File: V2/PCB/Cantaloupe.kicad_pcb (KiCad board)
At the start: 2 copper layers, 143.9 x 118.7 mm, 118 parts, among them J1 USB_In, J2 OLED, J3 Link, J4 Debug, J5 Trackball, Q1 2N7002, Q2 AO3401A, SW1 MX, SW10 MX, SW11 MX, SW12 MX, SW13 MX, SW14 MX, SW15 MX, SW16 MX, SW17 MX, SW18 MX, SW19 MX, SW2 MX, SW20 MX, SW21 MX, SW22 MX, SW23 MX, SW24 MX, SW25 MX, SW26 MX, SW27 MX, SW28 MX, SW29 MX, SW3 MX, SW30 MX, SW31 Encoder, SW32 MX, SW4 MX, SW5 MX, SW6 MX, SW7 MX, SW8 MX, SW9 MX, U1 STM32F4x1CxUx, U2 SRV05-4, U3 SRV05-4, U4 XC6206P332MR, U5 LMV321, Y1 8MHz

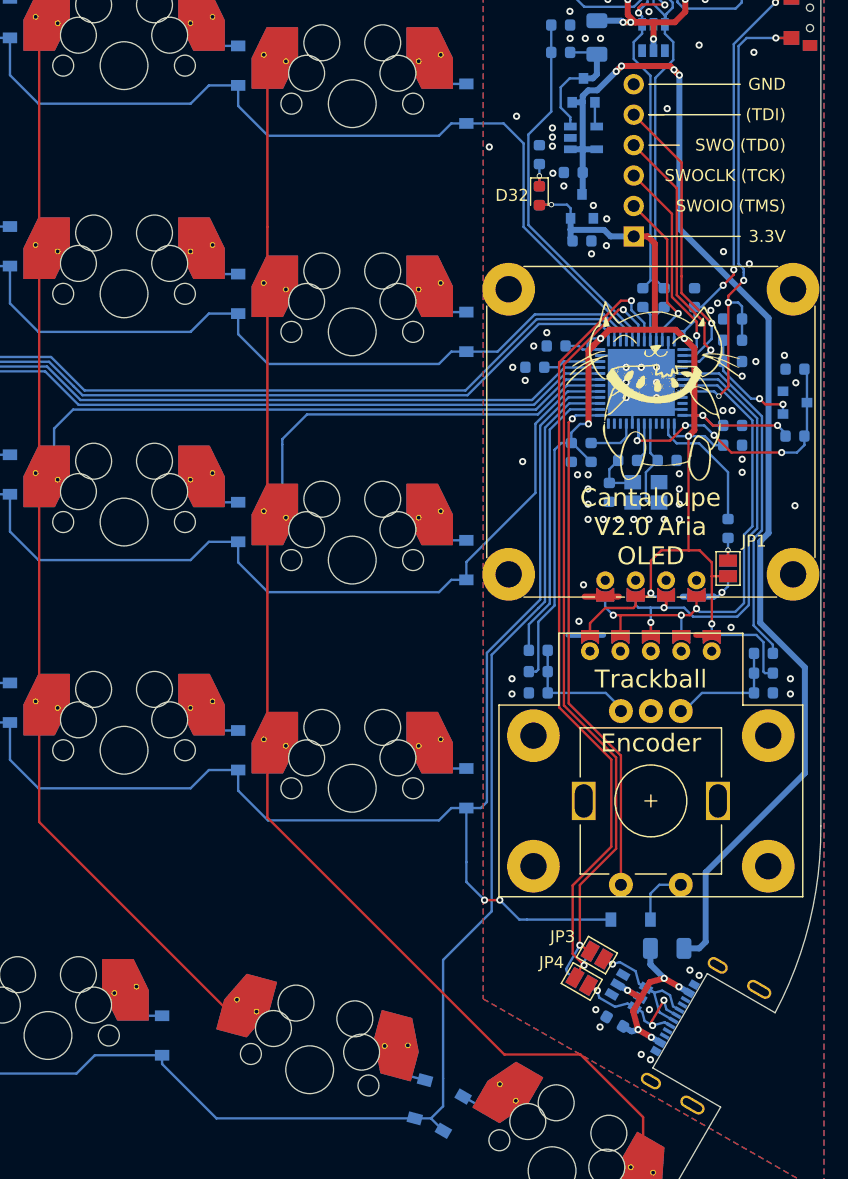
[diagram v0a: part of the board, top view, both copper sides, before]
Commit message: Fixed issues with PCB
Changed pin assignments so B2 isn't used. Added pull-up for RX pin and pull-down for B2 pin so it can properly load into the bootloader.
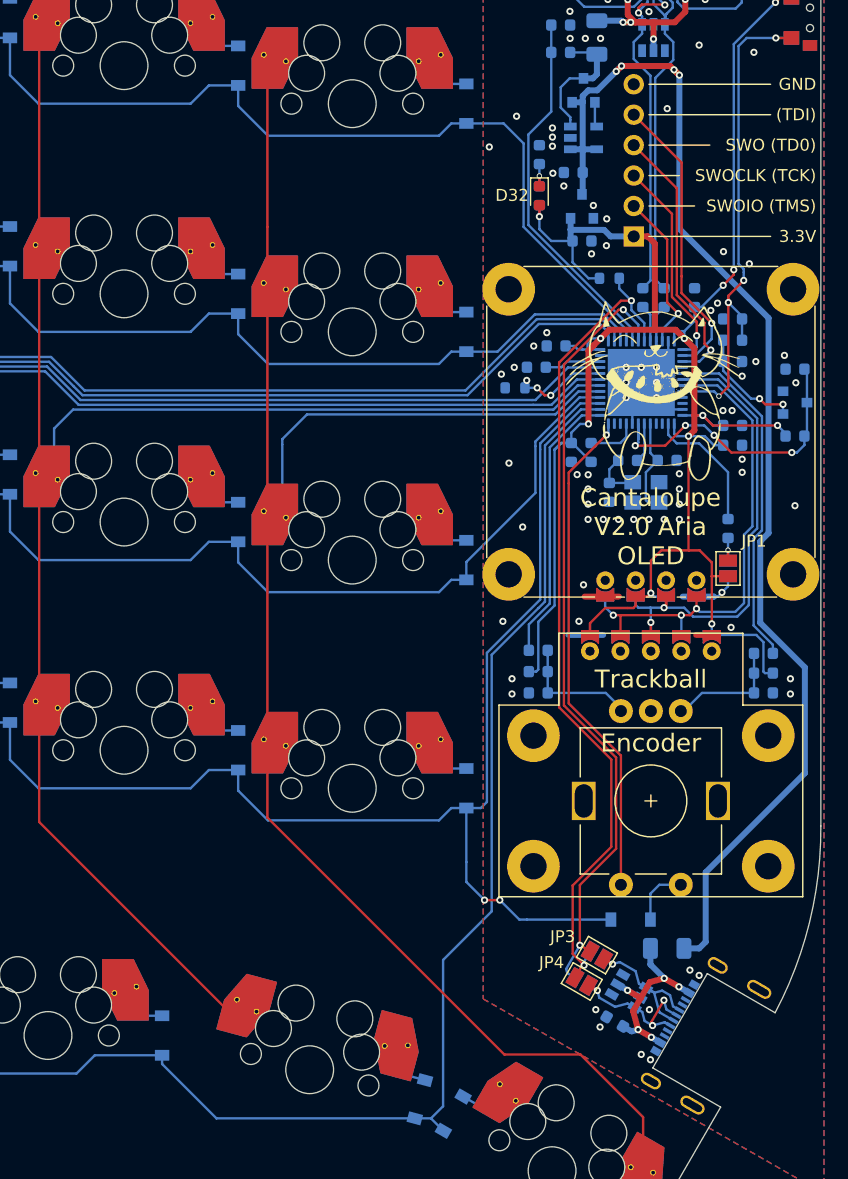
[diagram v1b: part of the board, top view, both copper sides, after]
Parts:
- added R18: 10k, Resistor_SMD:R_0603_1608Metric, B.Cu at (139.6, 44.9)
- added R4: 10k, Resistor_SMD:R_0603_1608Metric, B.Cu at (131.7, 54.0)
- moved C15 0.13 mm to (133.5, 52.3)
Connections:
- U1 pad 12: Net-(U1-Pad12) -> COLROT
- U1 pad 13: COLROT -> ROT_B
- U1 pad 14: ROT_B -> ROW4
- U1 pad 15: ROW4 -> ROW3
- U1 pad 16: ROW3 -> ROW2
- U1 pad 17: ROW2 -> COL5
- U1 pad 18: COL5 -> COL4
- U1 pad 19: COL4 -> COL3
- U1 pad 20: COL3 -> Net-(R4-Pad1)
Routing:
- net VDD: track 172.5 -> 180.1 mm
- net Net-(R4-Pad1): track 0.00 -> 7.29 mm, vias 0 -> 2
- net RX: track 68.5 -> 70.8 mm
- net COLROT: track 43.3 -> 41.7 mm
- net ROT_B: track 24.0 -> 23.0 mm
- net ROW4: track 169.6 -> 168.5 mm
- net ROW3: track 168.5 -> 167.4 mm
- net ROW2: track 129.7 -> 128.6 mm
- net NRST: track 25.0 -> 25.8 mm
- net GND: vias 84 -> 87
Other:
- rule pad_to_mask_clearance: 0.051 -> 0

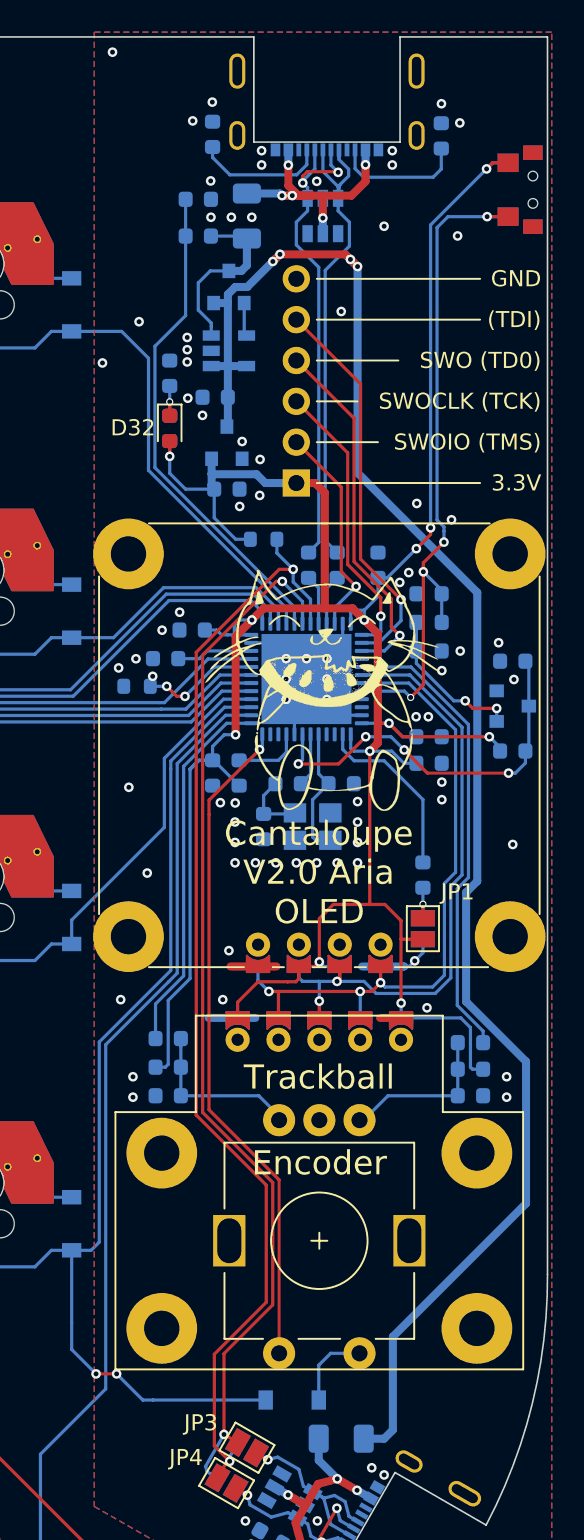
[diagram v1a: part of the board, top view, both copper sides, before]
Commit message: Fixed many issues with the board
Changed pin assignments so B2 isn't used. Added pull-up for RX pin and pull-down for B2 pin so the keyboard can properly load into the bootloader. Changed reset circuit so it actually works. Removed USB series resistors. Removed non-functional JTAG pins. Changed SRV05-04 to SRV0504. Thanks to sigprof and MasterSpoon from the QMK discord server for the help!
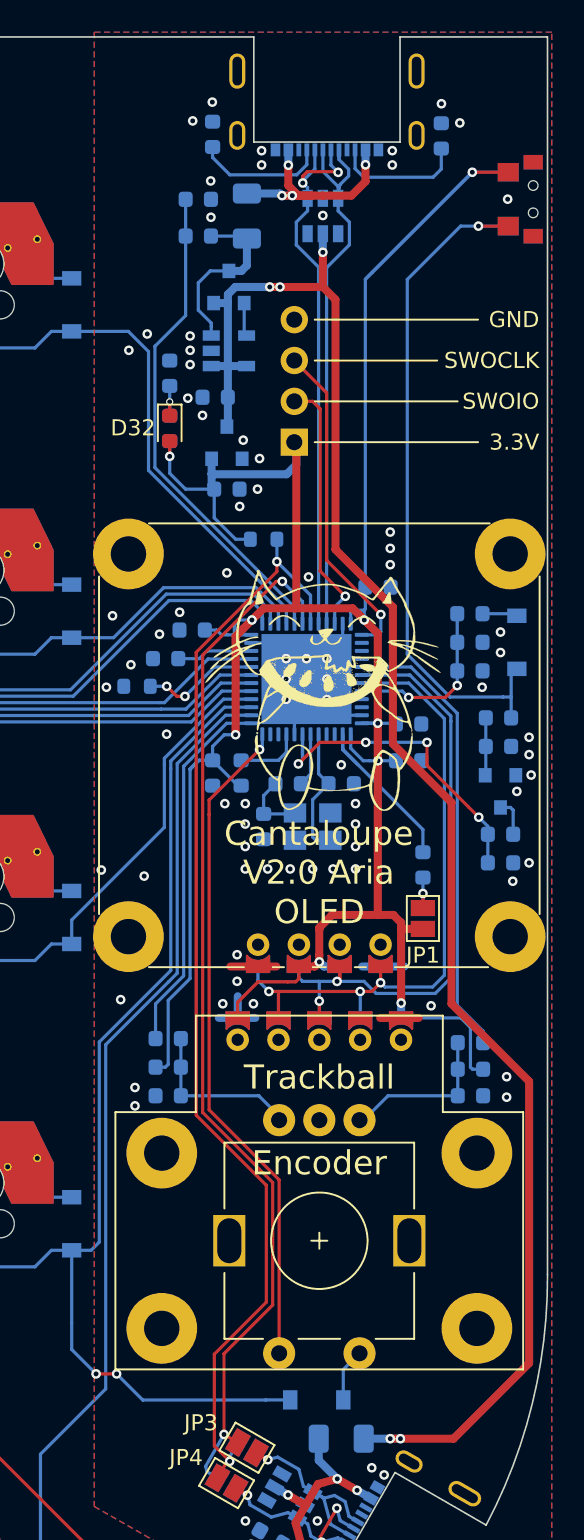
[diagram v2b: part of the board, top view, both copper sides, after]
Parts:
- added D33: D, Ariamelon:D_SOD-123, B.Cu at (155.3, 51.3)
- D32: moved to B.Cu
- R11: value 10k -> 1M
- R18, R4: value 10k -> 100k
- R2: value 10 -> 330k
- R3: value 10 -> 1k
- R9: value 100k -> 100
- U2, U3: value SRV05-4 -> SRV0504
- moved R3 13.8 mm to (154.2, 56.0), turned to 180 degrees
- moved C4 12.6 mm to (154.3, 65.0), turned to 180 degrees
- moved R9 12.2 mm to (154.3, 63.2), turned to 180 degrees
- moved R2 10.5 mm to (152.4, 49.5), turned to 0 degrees
- moved R7 10.4 mm to (154.2, 57.8), turned to 180 degrees
- moved R11 5.65 mm to (152.4, 53.1)
- moved Q1 5.36 mm to (154.3, 60.6), turned to 270 degrees
- moved C2 2.83 mm to (152.4, 51.3)
- moved D31 1.52 mm to (142.9, 98.4)
- moved C9 1.50 mm to (148.6, 56.4)
- moved C8 1.37 mm to (146.7, 47.9), turned to 180 degrees
- moved C14 1.28 mm to (148.6, 58.7)
- moved R16 0.64 mm to (149.5, 65.2)
- moved JP1 0.63 mm to (149.5, 68.5)
- moved JP2 0.63 mm to (149.5, 68.5)
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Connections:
- net JTCK renamed SWOCLK
- net JTMS renamed SWOIO
- C2 pad 1: Net-(C2-Pad1) -> BOOT0
- C2 pad 2: BOOT0 -> GND
- J4 pad 4: JTD0 -> GND
- Q1 pad 1: Net-(C2-Pad1) -> Net-(Q1-Pad1)
- Q1 pad 3: NRST -> Net-(Q1-Pad3)
- R11 pad 1: VDD -> BOOT0
- R11 pad 2: NRST -> GND
- R2 pad 1: D- -> BOOT0
- R2 pad 2: Net-(R2-Pad2) -> Net-(D33-Pad1)
- R3 pad 1: D+ -> Net-(D33-Pad2)
- R3 pad 2: Net-(R3-Pad2) -> Net-(Q1-Pad1)
- R7 pad 2: BOOT0 -> Net-(Q1-Pad1)
- R9 pad 1: Net-(C2-Pad1) -> Net-(Q1-Pad3)
- R9 pad 2: GND -> NRST
- SW32 pad 1: BOOT0 -> Net-(D33-Pad2)
- U1 pad 32: Net-(R2-Pad2) -> D-
- U1 pad 33: Net-(R3-Pad2) -> D+
- U1 pad 38: JTDI -> Net-(U1-Pad38)
- U1 pad 39: JTD0 -> Net-(U1-Pad39)
- U2 pad 5: VBUS -> VBUS_In
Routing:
- net Net-(D33-Pad2): track 0.00 -> 43.9 mm, vias 0 -> 1
- net BOOT0: track 43.1 -> 10.9 mm, vias 4 -> 2
- net JTDI: track 24.4 -> 0.00 mm, vias 1 -> 0
- net JTD0: track 22.5 -> 0.00 mm, vias 1 -> 0
- net Net-(C2-Pad1): track 9.51 -> 0.00 mm, vias 2 -> 0
- net VDD: track 180.1 -> 185.7 mm, vias 12 -> 9
- net NRST: track 25.8 -> 20.9 mm
- net D-: track 30.9 -> 35.1 mm
- net D+: track 30.1 -> 34.2 mm
- net Net-(Q1-Pad1): track 0.00 -> 3.59 mm
- net VBUS_In: track 105.4 -> 108.6 mm, vias 4 -> 5
- net Net-(R3-Pad2): track 3.13 -> 0.00 mm
- net Net-(R2-Pad2): track 3.11 -> 0.00 mm
- net SWOIO: track 13.4 -> 16.1 mm
- net SWOCLK: track 17.8 -> 20.4 mm
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
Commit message: Clean up of design. Added gerbers and files for FR4 plates.
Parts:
- C4: value 1u -> 100n
- D32: moved to F.Cu
- moved J4 5.21 mm to (146.7, 35.1)
- moved C6 2.29 mm to (138.8, 36.1)
- moved C7 2.29 mm to (139.6, 41.8)
- moved D32 2.29 mm to (136.0, 38.0)
- moved R15 2.29 mm to (136.0, 34.6)
- moved U4 2.29 mm to (139.6, 38.9)
- moved Q2 2.29 mm to (139.7, 29.2)
- moved U5 2.29 mm to (139.7, 33.2)
- moved F1 0.63 mm to (145.0, 100.8)
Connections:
- net SWOCLK renamed SWCLK
- net SWOIO renamed SWDIO
- F2 pad 1: Net-(F2-Pad1) -> VBUS_Fused
- Q2 pad 3: Net-(F2-Pad1) -> VBUS_Fused
- R13 pad 1: Net-(F2-Pad1) -> VBUS_Fused
- U2 pad 5: VBUS_In -> VBUS_Fused
- U5 pad 3: Net-(F2-Pad1) -> VBUS_Fused
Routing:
- net VDD: track 185.7 -> 168.7 mm, vias 9 -> 10
- net VBUS_Fused: track 0.00 -> 15.6 mm, vias 0 -> 2
- net Net-(F2-Pad1): track 11.3 -> 0.00 mm
- net VBUS_In: track 108.6 -> 97.6 mm, vias 5 -> 4
- net Net-(D33-Pad2): track 43.9 -> 42.3 mm
- net PLUGGED: track 30.8 -> 29.2 mm
- net TX: track 66.8 -> 67.9 mm
- net COL1: track 192.8 -> 191.8 mm
- net RX: track 70.6 -> 71.5 mm
- net SWCLK: track 20.4 -> 19.6 mm
- net ROW0: track 133.5 -> 134.3 mm
- net SWDIO: track 16.1 -> 16.7 mm
- net GND: vias 85 -> 84

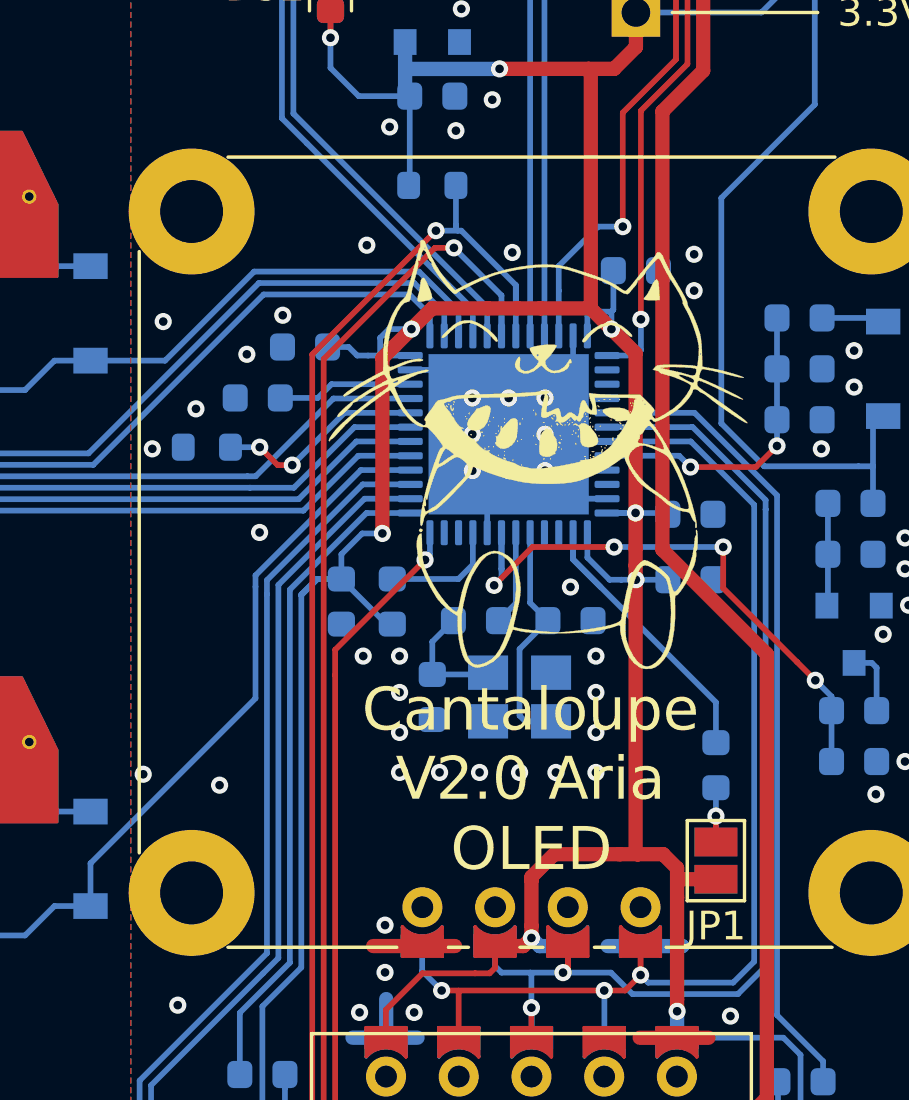
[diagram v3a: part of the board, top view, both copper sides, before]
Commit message: Fixed jumper side
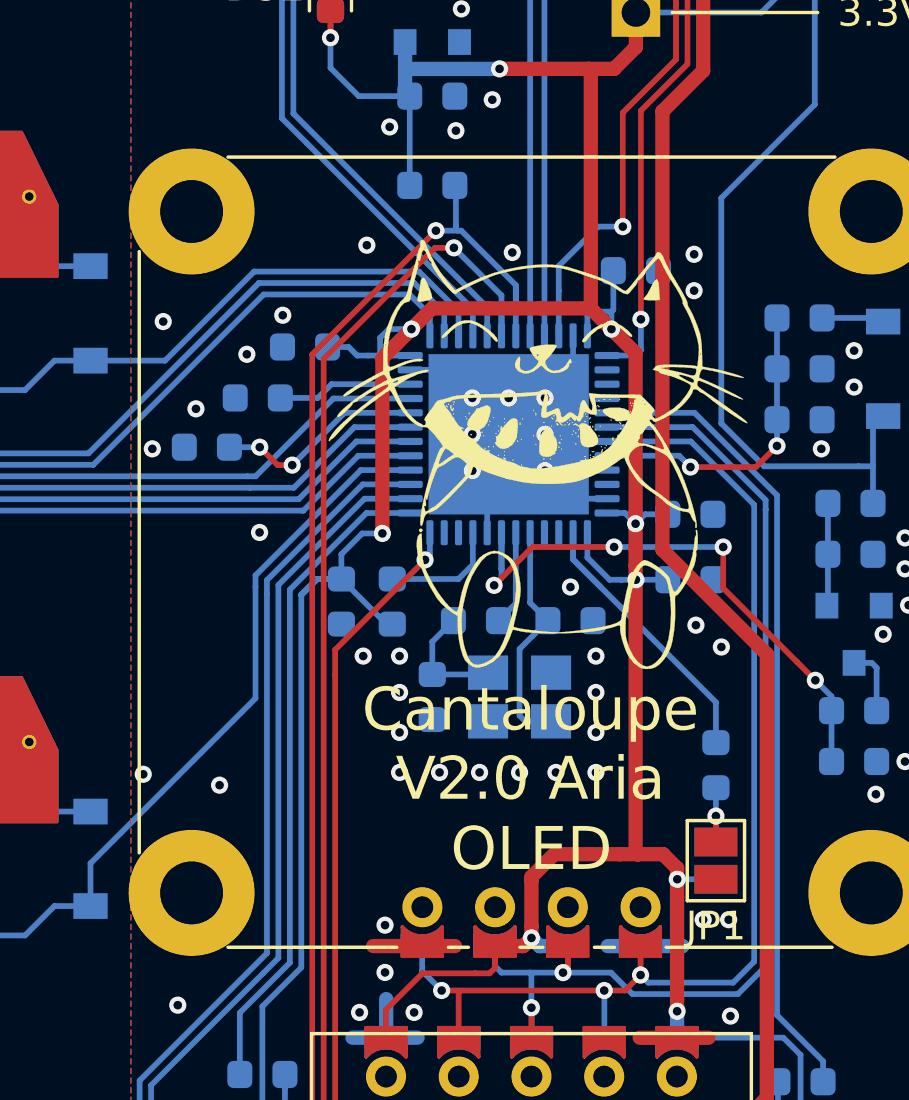
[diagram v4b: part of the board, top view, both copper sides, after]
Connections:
- JP1 pad 1: VDD -> GND
- JP2 pad 1: GND -> VDD
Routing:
- net VDD: track 168.7 -> 168.0 mm, vias 10 -> 11
- net GND: vias 84 -> 88

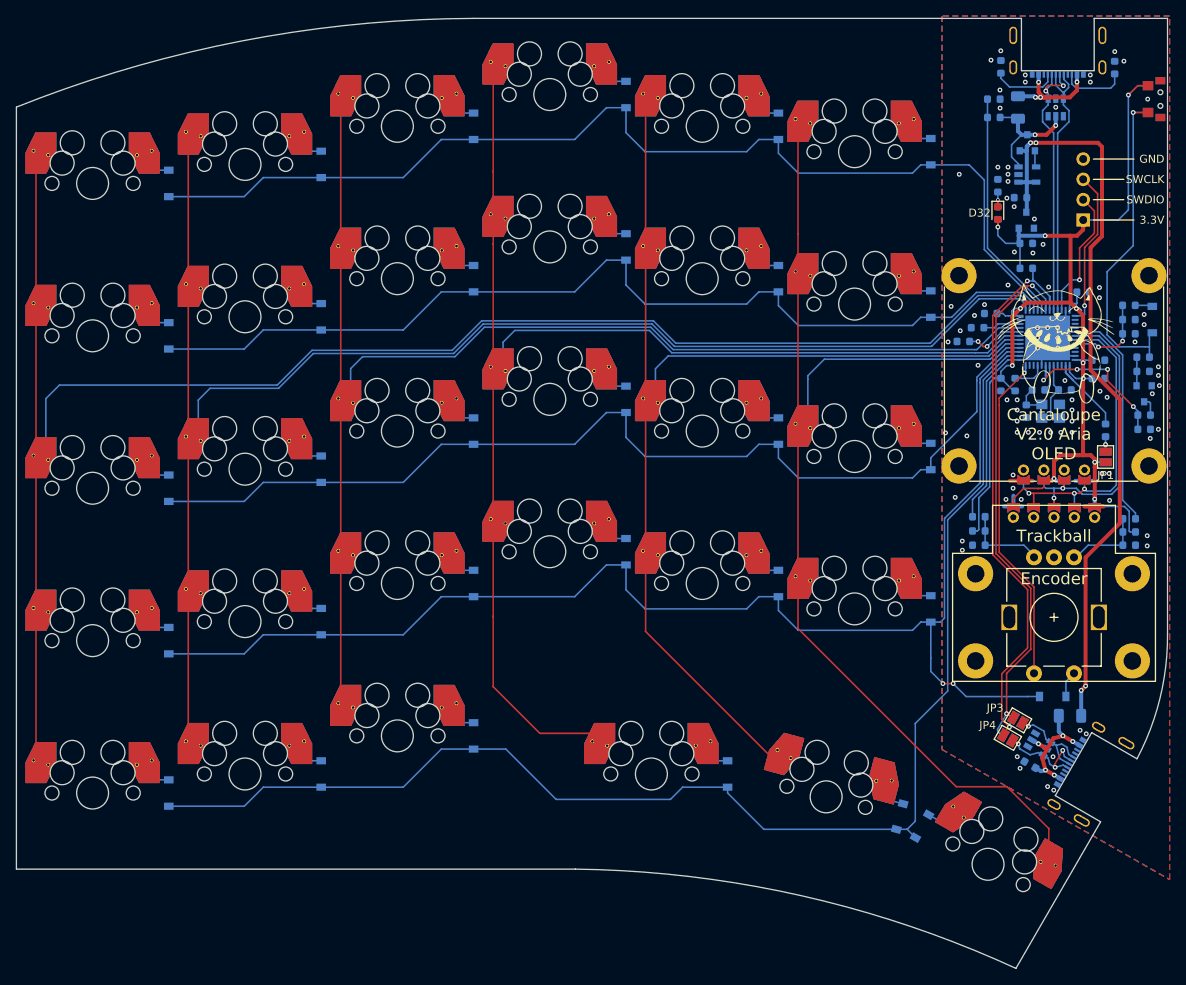
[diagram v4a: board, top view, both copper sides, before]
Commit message: Finalized firmware. Added custom graphic to OLED display. Updated 3DP case and BOM. Fixed error with silkscreen.
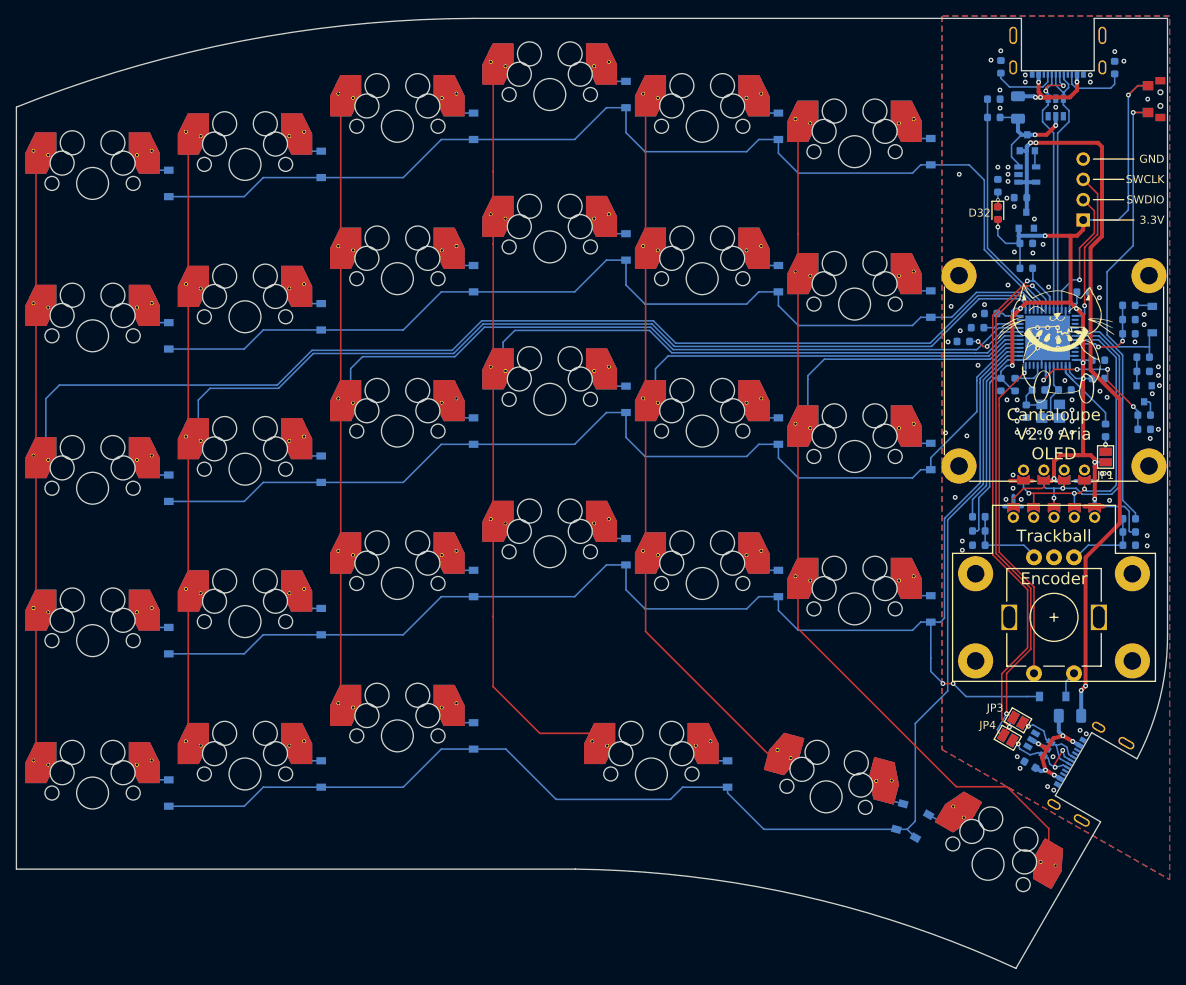
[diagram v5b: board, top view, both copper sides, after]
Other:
- net class Default removed
- net class Power removed
